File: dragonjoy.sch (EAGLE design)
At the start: 12 parts, among them IC1 4066N

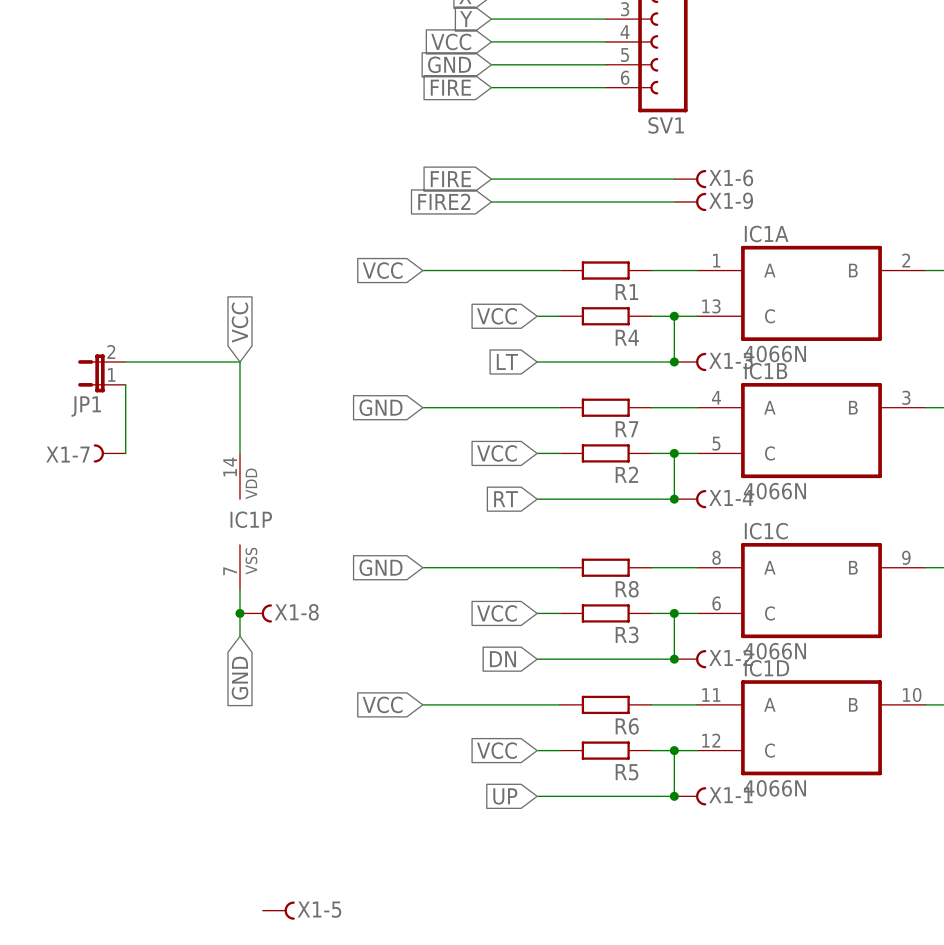
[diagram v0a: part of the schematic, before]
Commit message: add 90 degree connector
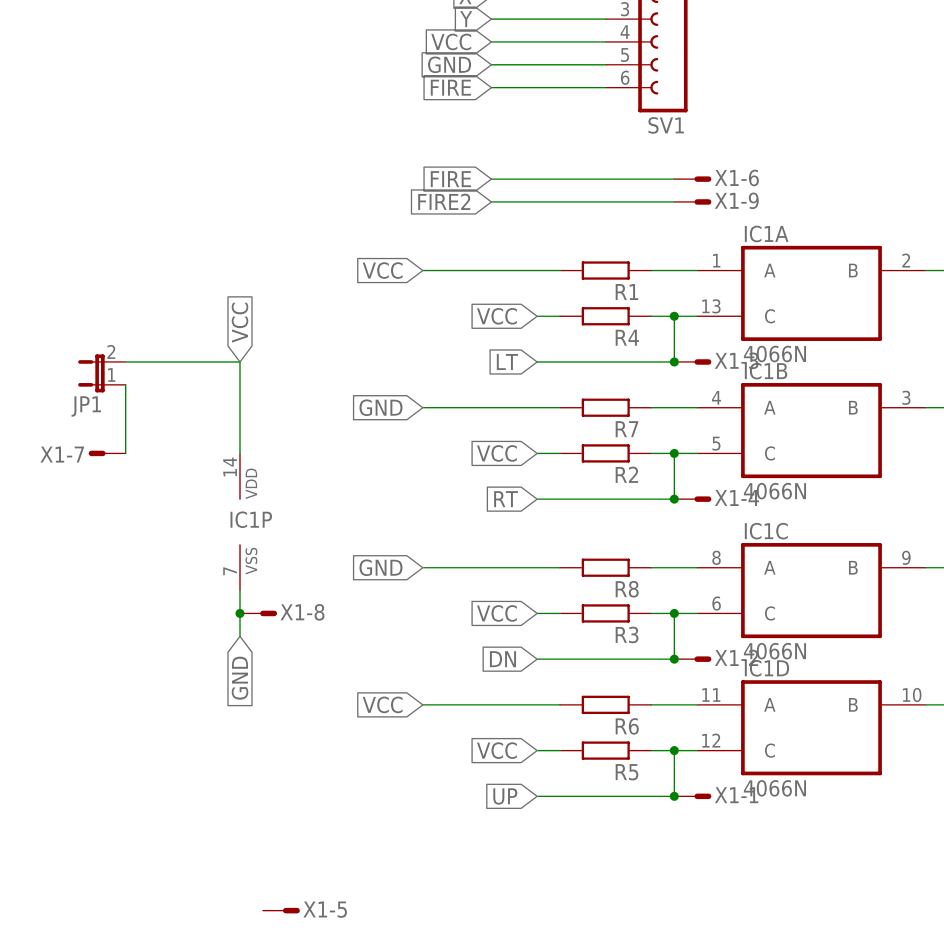
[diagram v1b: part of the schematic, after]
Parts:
- X1: device con-subd:F09VPS -> con-subd:M09-182S
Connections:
- net DN: now also X1-2.M; no longer X1-2.F
- net FIRE: now also X1-6.M; no longer X1-6.F
- net FIRE2: now also X1-9.M; no longer X1-9.F
- net GND: now also X1-8.M; no longer X1-8.F
- net LT: now also X1-3.M; no longer X1-3.F
- net N$1: now also X1-7.M; no longer X1-7.F
- net RT: now also X1-4.M; no longer X1-4.F
- net UP: now also X1-1.M; no longer X1-1.F
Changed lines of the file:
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@@
 <part name="R7" library="rcl" deviceset="R-EU_" device="0207/10"/>
 <part name="R8" library="rcl" deviceset="R-EU_" device="0207/10"/>
-<part name="X1" library="con-subd" deviceset="F09?S" device="VP"/>
+<part name="X1" library="con-subd" deviceset="M09?S" device="-182"/>
 <part name="SV1" library="con-lsta" deviceset="FE06-1" device=""/>
 <part name="JP1" library="jumper" deviceset="JP1E" device=""/>
@@
 <wire x1="-10.16" y1="53.34" x2="-25.4" y2="53.34" width="0.1524" layer="91"/>
 <label x="-25.4" y="53.34" size="1.778" layer="95" rot="R180" xref="yes"/>
-<pinref part="X1" gate="-4" pin="F"/>
+<pinref part="X1" gate="-4" pin="M"/>
 <junction x="-10.16" y="53.34"/>
 </segment>
@@
 <wire x1="-10.16" y1="35.56" x2="-25.4" y2="35.56" width="0.1524" layer="91"/>
 <label x="-25.4" y="35.56" size="1.778" layer="95" rot="R180" xref="yes"/>
-<pinref part="X1" gate="-2" pin="F"/>
+<pinref part="X1" gate="-2" pin="M"/>
 <junction x="-10.16" y="35.56"/>
 </segment>
@@
 <wire x1="-10.16" y1="68.58" x2="-25.4" y2="68.58" width="0.1524" layer="91"/>
 <label x="-25.4" y="68.58" size="1.778" layer="95" rot="R180" xref="yes"/>
-<pinref part="X1" gate="-3" pin="F"/>
+<pinref part="X1" gate="-3" pin="M"/>
 <junction x="-10.16" y="68.58"/>
 </segment>
@@
 <wire x1="-10.16" y1="20.32" x2="-25.4" y2="20.32" width="0.1524" layer="91"/>
 <label x="-25.4" y="20.32" size="1.778" layer="95" rot="R180" xref="yes"/>
-<pinref part="X1" gate="-1" pin="F"/>
+<pinref part="X1" gate="-1" pin="M"/>
 <junction x="-10.16" y="20.32"/>
 </segment>
@@
 <wire x1="-58.42" y1="43.18" x2="-58.42" y2="40.64" width="0.1524" layer="91"/>
 <label x="-58.42" y="38.1" size="1.778" layer="95" rot="R270" xref="yes"/>
-<pinref part="X1" gate="-8" pin="F"/>
+<pinref part="X1" gate="-8" pin="M"/>
 <wire x1="-58.42" y1="40.64" x2="-58.42" y2="38.1" width="0.1524" layer="91"/>
 <junction x="-58.42" y="40.64"/>
@@
 <net name="FIRE" class="0">
 <segment>
-<pinref part="X1" gate="-6" pin="F"/>
+<pinref part="X1" gate="-6" pin="M"/>
 <wire x1="-10.16" y1="88.9" x2="-30.48" y2="88.9" width="0.1524" layer="91"/>
 <label x="-30.48" y="88.9" size="1.778" layer="95" rot="R180" xref="yes"/>
@@
 <net name="FIRE2" class="0">
 <segment>
-<pinref part="X1" gate="-9" pin="F"/>
+<pinref part="X1" gate="-9" pin="M"/>
 <wire x1="-10.16" y1="86.36" x2="-30.48" y2="86.36" width="0.1524" layer="91"/>
 <label x="-30.48" y="86.36" size="1.778" layer="95" rot="R180" xref="yes"/>
@@
 <pinref part="JP1" gate="A" pin="1"/>
 <wire x1="-71.12" y1="66.04" x2="-71.12" y2="58.42" width="0.1524" layer="91"/>
-<pinref part="X1" gate="-7" pin="F"/>
-</segment>
-</net>
+<pinref part="X1" gate="-7" pin="M"/>
+</segment>
+</net>

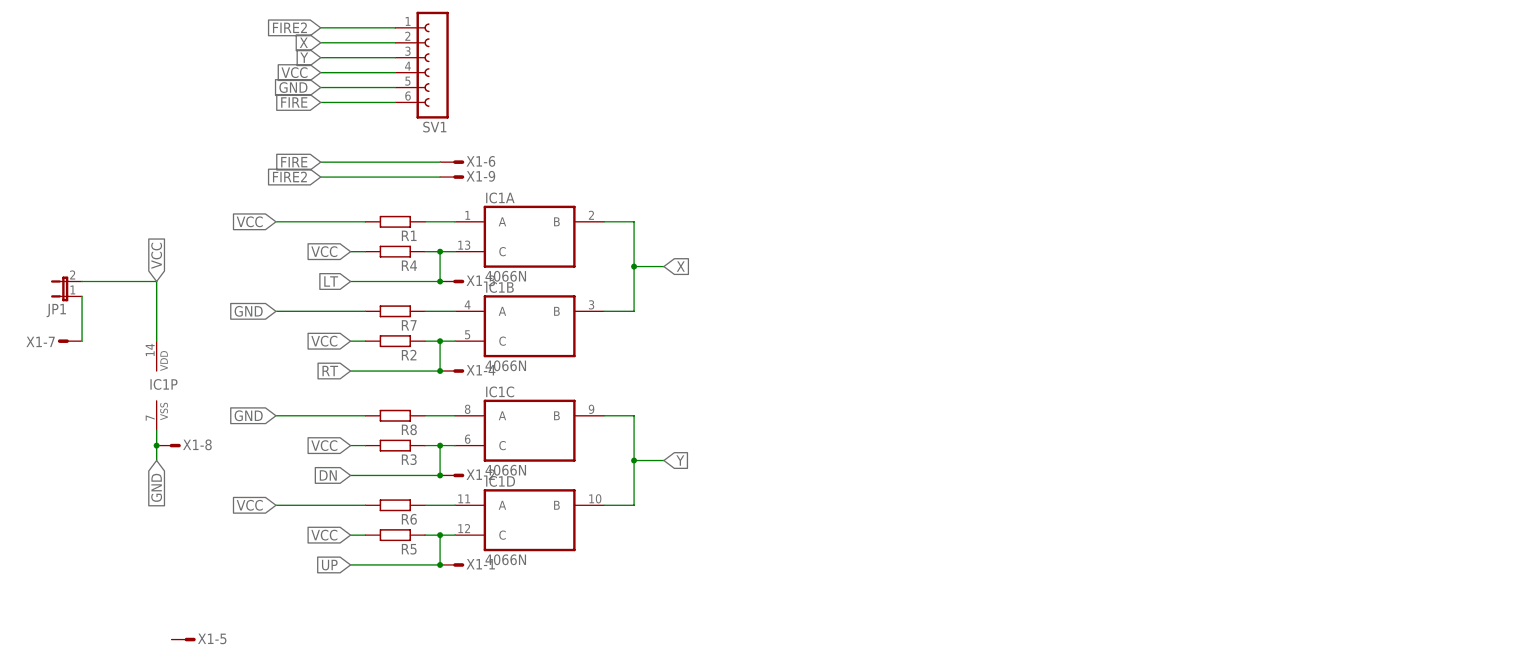
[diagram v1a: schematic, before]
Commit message: double up board elements at schematic level
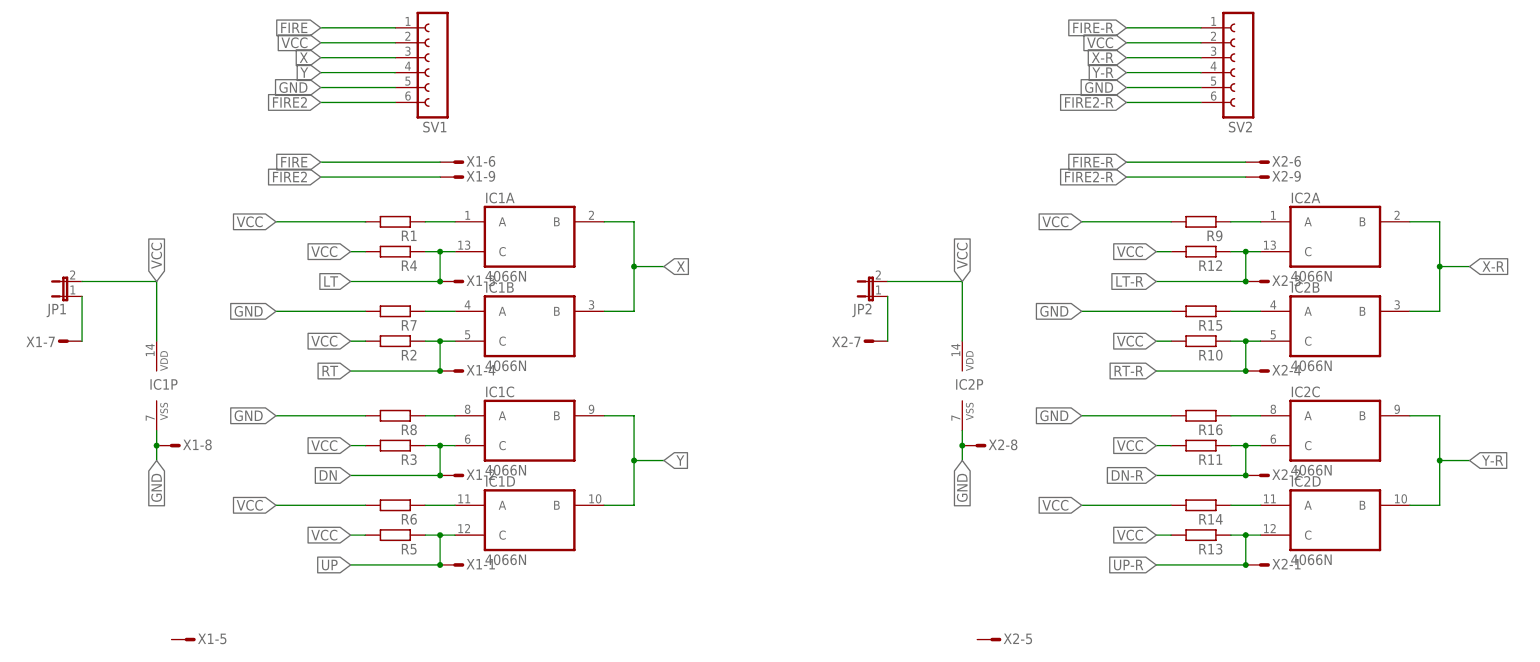
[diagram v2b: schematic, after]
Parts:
- added IC2: 4066N, 40xx:4066N
- added JP2: (no value), jumper:JP1E
- added R10, R11, R12, R13, R14, R15, R16, R9: (no value), rcl:R-EU_0207/10
- added SV2: (no value), con-lsta:FE06-1
- added X2: (no value), con-subd:M09-182S
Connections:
- new net DN-R: IC2C.C, R11.1, X2-2.M
- new net FIRE-R: SV2.1, X2-6.M
- new net FIRE2-R: SV2.6, X2-9.M
- new net LT-R: IC2A.C, R12.1, X2-3.M
- new net N$2: IC2A.A, R9.1
- new net N$4: IC2D.A, R14.1
- new net N$5: IC2B.A, R15.1
- new net N$6: IC2C.A, R16.1
- new net N$7: JP2.1, X2-7.M
- new net RT-R: IC2B.C, R10.1, X2-4.M
- new net UP-R: IC2D.C, R13.1, X2-1.M
- new net X-R: IC2A.B, IC2B.B, SV2.3
- new net Y-R: IC2C.B, IC2D.B, SV2.4
- net FIRE: now also SV1.1; no longer SV1.6
- net FIRE2: now also SV1.6; no longer SV1.1
- net GND: now also IC2P.VSS, R15.2, R16.2, SV2.5, X2-8.M
- net VCC: now also IC2P.VDD, JP2.2, R10.2, R11.2, R12.2, R13.2, R14.2, R9.2, SV1.2, SV2.2; no longer SV1.4
- net X: now also SV1.3; no longer SV1.2
- net Y: now also SV1.4; no longer SV1.3

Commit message: prepare for submission
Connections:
- net N$7 renamed N$7-R
- new net VCC-R: IC2P.VDD, JP2.2, R10.2, R11.2, R12.2, R13.2, R14.2, R9.2, SV2.2
- net VCC: no longer IC2P.VDD, JP2.2, R10.2, R11.2, R12.2, R13.2, R14.2, R9.2, SV2.2
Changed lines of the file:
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@@
 <label x="-58.42" y="68.58" size="1.778" layer="95" rot="R90" xref="yes"/>
-</segment>
-<segment>
-<pinref part="R9" gate="G$1" pin="2"/>
-<wire x1="114.3" y1="78.74" x2="99.06" y2="78.74" width="0.1524" layer="91"/>
-<label x="99.06" y="78.74" size="1.778" layer="95" rot="R180" xref="yes"/>
-</segment>
-<segment>
-<pinref part="R10" gate="G$1" pin="2"/>
-<wire x1="114.3" y1="58.42" x2="111.76" y2="58.42" width="0.1524" layer="91"/>
-<label x="111.76" y="58.42" size="1.778" layer="95" rot="R180" xref="yes"/>
-</segment>
-<segment>
-<pinref part="R11" gate="G$1" pin="2"/>
-<wire x1="114.3" y1="40.64" x2="111.76" y2="40.64" width="0.1524" layer="91"/>
-<label x="111.76" y="40.64" size="1.778" layer="95" rot="R180" xref="yes"/>
-</segment>
-<segment>
-<wire x1="114.3" y1="30.48" x2="99.06" y2="30.48" width="0.1524" layer="91"/>
-<label x="99.06" y="30.48" size="1.778" layer="95" rot="R180" xref="yes"/>
-<pinref part="R14" gate="G$1" pin="2"/>
-</segment>
-<segment>
-<wire x1="114.3" y1="25.4" x2="111.76" y2="25.4" width="0.1524" layer="91"/>
-<label x="111.76" y="25.4" size="1.778" layer="95" rot="R180" xref="yes"/>
-<pinref part="R13" gate="G$1" pin="2"/>
-</segment>
-<segment>
-<wire x1="114.3" y1="73.66" x2="111.76" y2="73.66" width="0.1524" layer="91"/>
-<label x="111.76" y="73.66" size="1.778" layer="95" rot="R180" xref="yes"/>
-<pinref part="R12" gate="G$1" pin="2"/>
-</segment>
-<segment>
-<wire x1="119.38" y1="109.22" x2="106.68" y2="109.22" width="0.1524" layer="91"/>
-<label x="106.68" y="109.22" size="1.778" layer="95" rot="R180" xref="yes"/>
-<pinref part="SV2" gate="G$1" pin="2"/>
-</segment>
-<segment>
-<pinref part="JP2" gate="A" pin="2"/>
-<pinref part="IC2" gate="P" pin="VDD"/>
-<wire x1="66.04" y1="68.58" x2="78.74" y2="68.58" width="0.1524" layer="91"/>
-<wire x1="78.74" y1="68.58" x2="78.74" y2="58.42" width="0.1524" layer="91"/>
-<label x="78.74" y="68.58" size="1.778" layer="95" rot="R90" xref="yes"/>
 </segment>
 </net>
@@
 </segment>
 </net>
-<net name="N$7" class="0">
+<net name="N$7-R" class="0">
 <segment>
 <pinref part="JP2" gate="A" pin="1"/>
@@
 </segment>
 </net>
+<net name="VCC-R" class="0">
+<segment>
+<wire x1="119.38" y1="109.22" x2="106.68" y2="109.22" width="0.1524" layer="91"/>
+<label x="106.68" y="109.22" size="1.778" layer="95" rot="R180" xref="yes"/>
+<pinref part="SV2" gate="G$1" pin="2"/>
+</segment>
+<segment>
+<pinref part="R9" gate="G$1" pin="2"/>
+<wire x1="114.3" y1="78.74" x2="99.06" y2="78.74" width="0.1524" layer="91"/>
+<label x="99.06" y="78.74" size="1.778" layer="95" rot="R180" xref="yes"/>
+</segment>
+<segment>
+<wire x1="114.3" y1="73.66" x2="111.76" y2="73.66" width="0.1524" layer="91"/>
+<label x="111.76" y="73.66" size="1.778" layer="95" rot="R180" xref="yes"/>
+<pinref part="R12" gate="G$1" pin="2"/>
+</segment>
+<segment>
+<pinref part="R10" gate="G$1" pin="2"/>
+<wire x1="114.3" y1="58.42" x2="111.76" y2="58.42" width="0.1524" layer="91"/>
+<label x="111.76" y="58.42" size="1.778" layer="95" rot="R180" xref="yes"/>
+</segment>
+<segment>
+<pinref part="R11" gate="G$1" pin="2"/>
+<wire x1="114.3" y1="40.64" x2="111.76" y2="40.64" width="0.1524" layer="91"/>
+<label x="111.76" y="40.64" size="1.778" layer="95" rot="R180" xref="yes"/>
+</segment>
+<segment>
+<wire x1="114.3" y1="25.4" x2="111.76" y2="25.4" width="0.1524" layer="91"/>
+<label x="111.76" y="25.4" size="1.778" layer="95" rot="R180" xref="yes"/>
+<pinref part="R13" gate="G$1" pin="2"/>
+</segment>
+<segment>
+<pinref part="JP2" gate="A" pin="2"/>
+<pinref part="IC2" gate="P" pin="VDD"/>
+<wire x1="66.04" y1="68.58" x2="78.74" y2="68.58" width="0.1524" layer="91"/>
+<wire x1="78.74" y1="68.58" x2="78.74" y2="58.42" width="0.1524" layer="91"/>
+<label x="78.74" y="68.58" size="1.778" layer="95" rot="R90" xref="yes"/>
+</segment>
+<segment>
+<wire x1="114.3" y1="30.48" x2="99.06" y2="30.48" width="0.1524" layer="91"/>
+<label x="99.06" y="30.48" size="1.778" layer="95" rot="R180" xref="yes"/>
+<pinref part="R14" gate="G$1" pin="2"/>
+</segment>
+</net>
